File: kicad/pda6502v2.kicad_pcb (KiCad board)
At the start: 4 copper layers, 100 x 100 mm, 89 parts, among them J1 GPIO1, J2 GPIO2, J3 UART, J4 Screw_Terminal_01x02, J5 Conn_02x04_Odd_Even, J6 ICSP, J7 SPI, J8 FPGA_EXT, J9 SID, SW1 SW_Push, U1 W65C02SxP, U10 LT3030, U11 SC28L92A1B, U2 W65C22SxP, U3 W65C22SxP, U4 DS1818, U5 AS6C4008-55PCN, U6 ARMSID, U7 AT25M01, U8 ICE40HX4K-TQ144, U9 TLV1117-33, X1 8 MHz, X2 3.6864 MHz

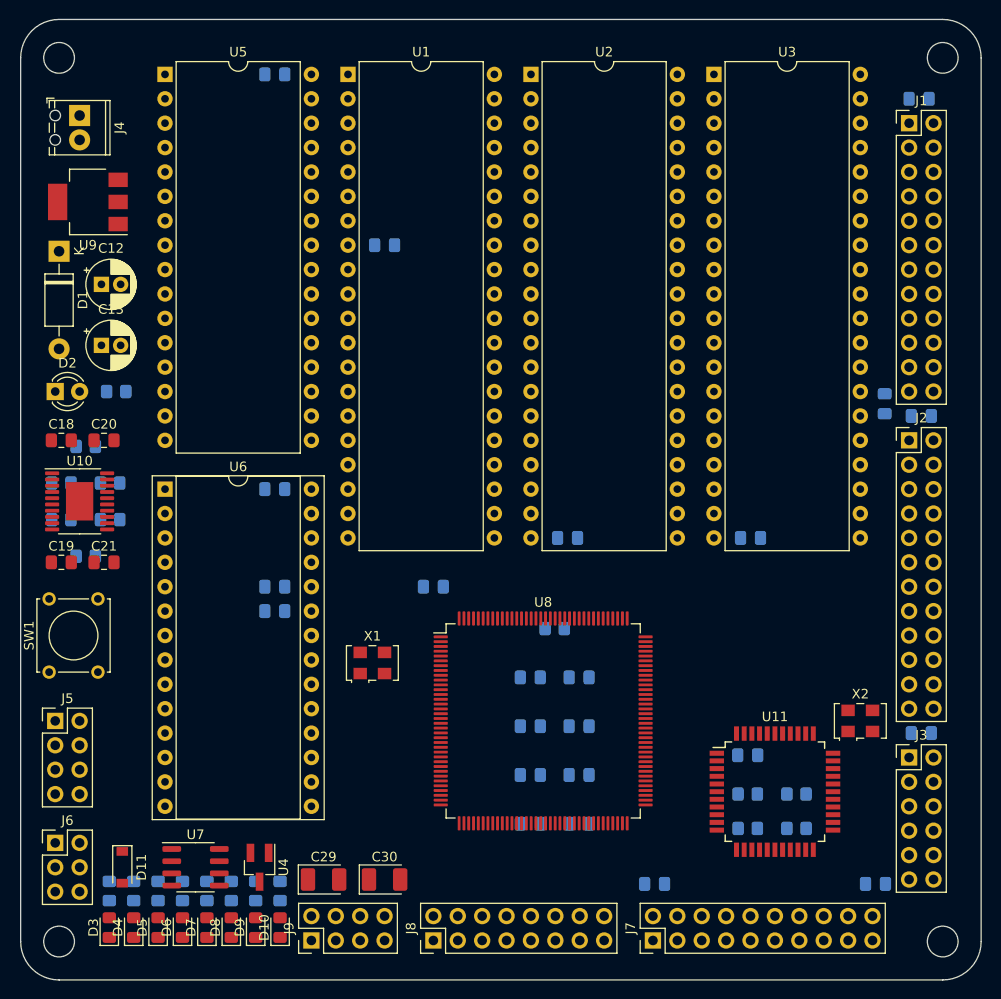
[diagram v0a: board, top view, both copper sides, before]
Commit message: Routing begins; FPGA to EXT & SPI headers.
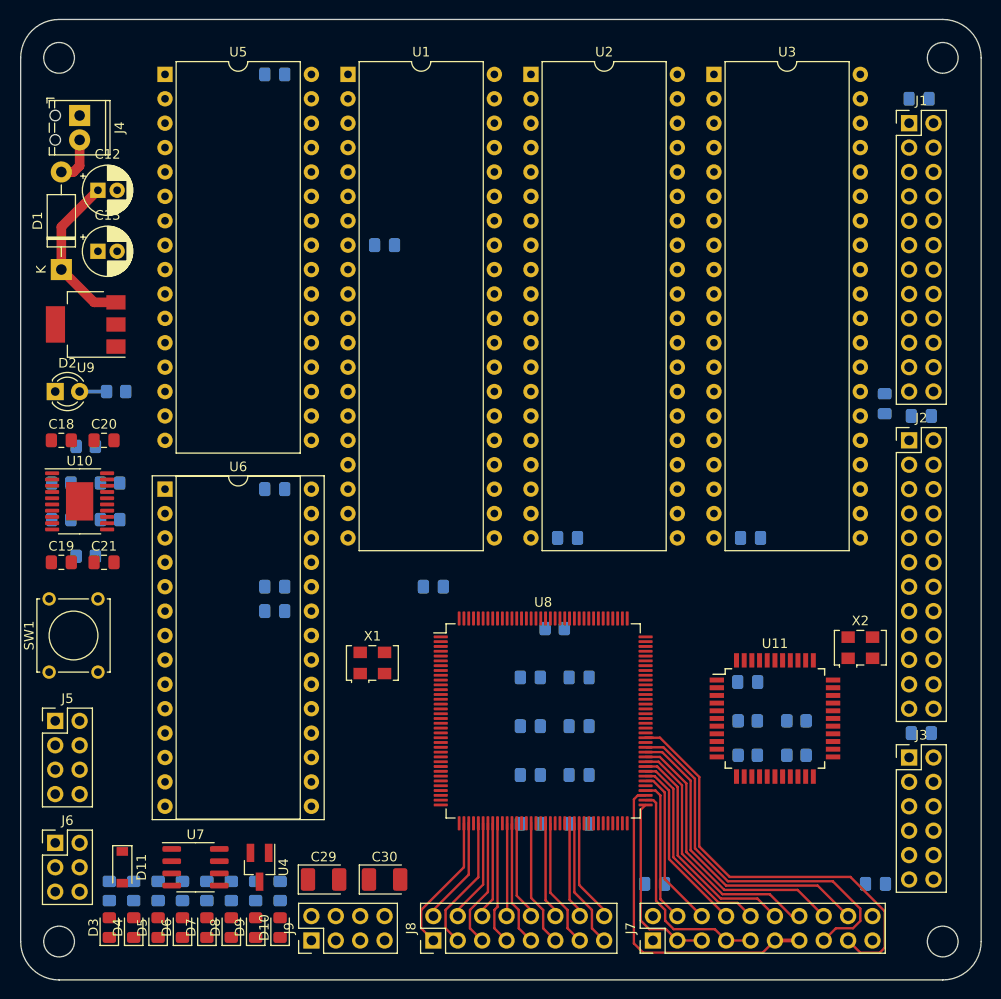
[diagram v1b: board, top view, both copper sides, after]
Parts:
- moved U9 12.8 mm to (104.8, 71.8)
- moved C12 9.80 mm to (106.0, 57.8)
- moved C13 9.80 mm to (106.0, 64.1)
- moved C3 7.62 mm to (173.7, 109.0)
- moved R1 7.62 mm to (173.7, 113.0)
- moved R2 7.62 mm to (178.8, 113.0)
- moved U11 7.62 mm to (176.5, 112.8)
- moved X2 7.62 mm to (185.4, 105.4)
- moved R3 7.62 mm to (173.7, 116.6)
- moved R4 7.62 mm to (178.8, 116.6)
- moved D1 1.92 mm to (102.2, 66.0), turned to 90 degrees
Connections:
- J4 pad 1: Net-(D1-Pad2) -> GND
- J4 pad 2: GND -> Net-(D1-Pad2)
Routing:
- net /SPI_EXP1: track 0.00 -> 45.8 mm
- net /SPI_EXP0: track 0.00 -> 39.5 mm
- net /SPI_CLOCK: track 0.00 -> 34.5 mm
- net /SPI_CS7: track 0.00 -> 32.4 mm
- net /SPI_CS6: track 0.00 -> 29.6 mm
- net /SPI_CS5: track 0.00 -> 26.8 mm
- net /SPI_CS4: track 0.00 -> 24.1 mm
- net /SPI_MOSI: track 0.00 -> 23.6 mm
- net /SPI_CS3: track 0.00 -> 21.3 mm
- net /SPI_MISO: track 0.00 -> 19.5 mm
- net /SPI_CS2: track 0.00 -> 18.6 mm
- net /SPI_CS1: track 0.00 -> 17.6 mm
- net +5V: track 0.00 -> 16.9 mm
- net /SPI_CS0: track 0.00 -> 15.0 mm
- net /EXT_0: track 0.00 -> 14.6 mm
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
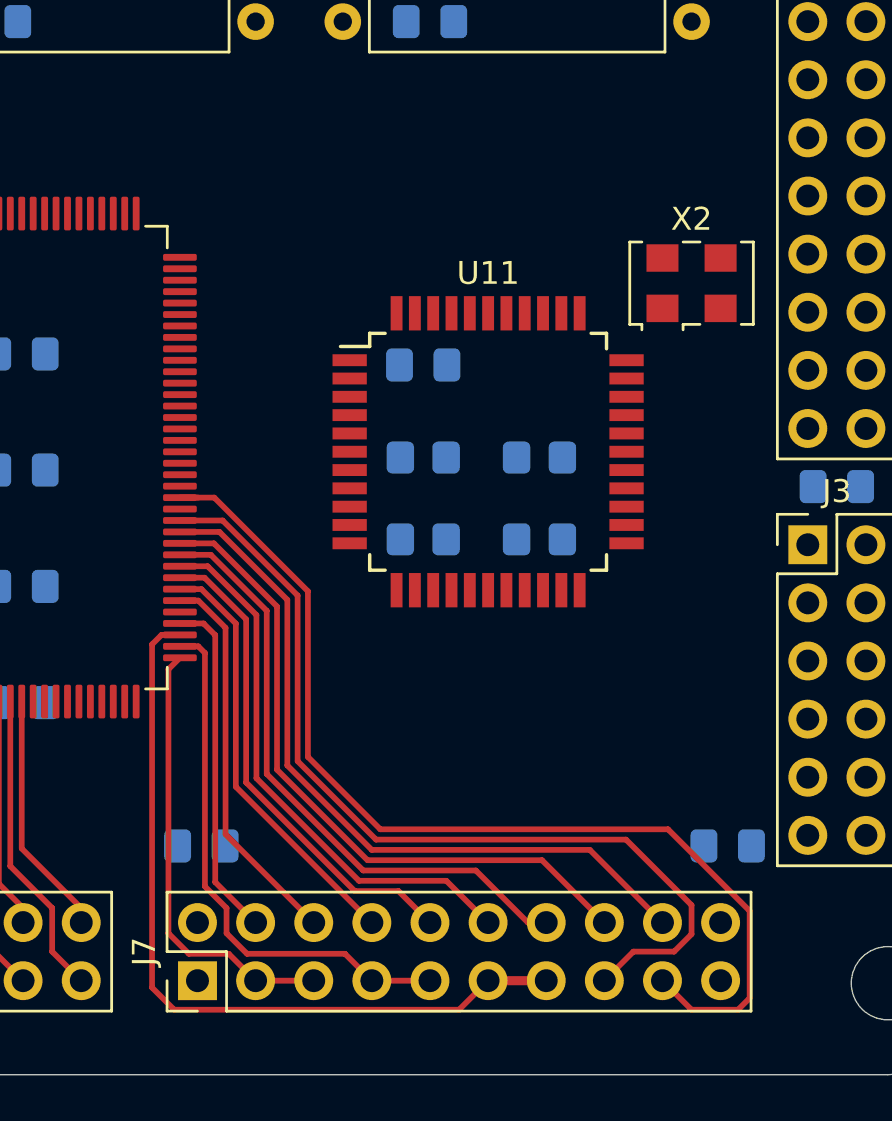
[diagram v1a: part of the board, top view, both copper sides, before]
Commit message: FPGA EXT/SPI routing tweaks, UART moved down/right
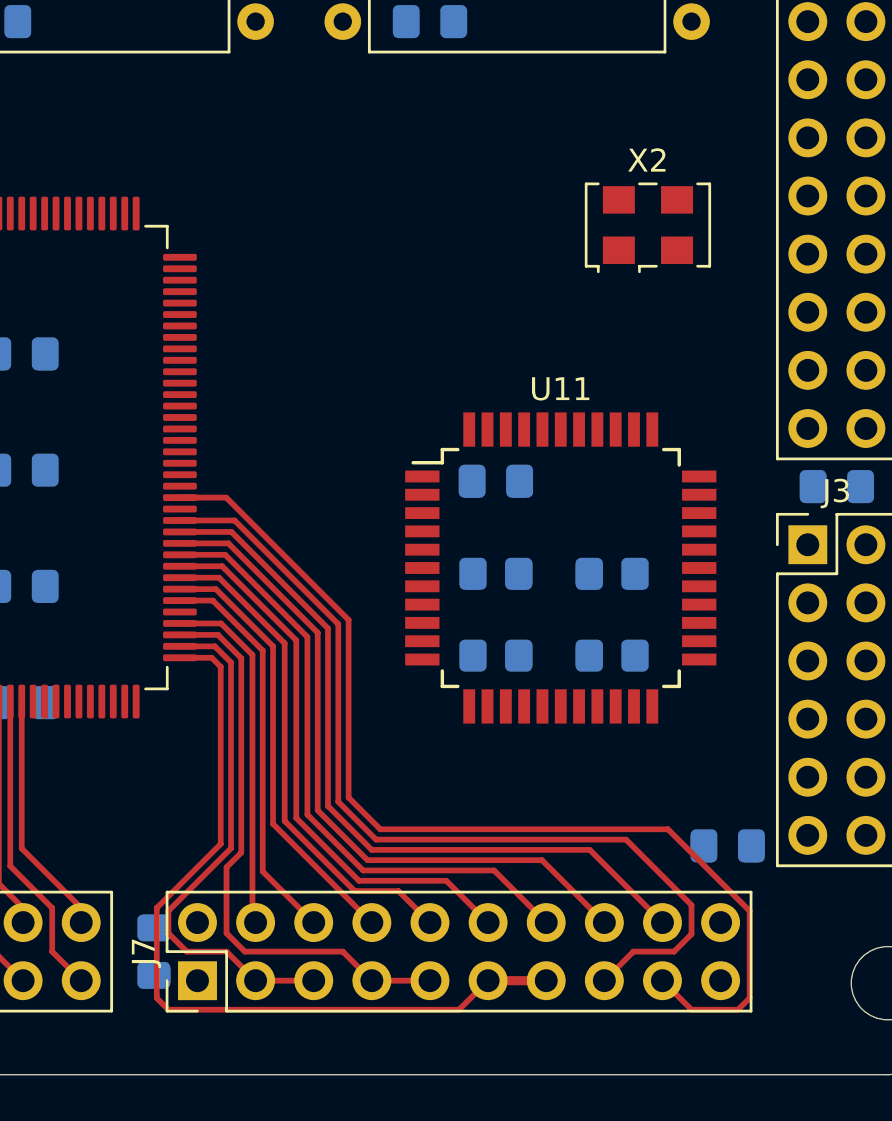
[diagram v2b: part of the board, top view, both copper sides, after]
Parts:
- moved C3 5.99 mm to (176.9, 114.1)
- moved R1 5.99 mm to (176.9, 118.1)
- moved R3 5.99 mm to (176.9, 121.7)
- moved U11 5.99 mm to (179.7, 117.9)
- moved R2 5.99 mm to (181.9, 118.1)
- moved R4 5.99 mm to (181.9, 121.7)
- moved C26 5.06 mm to (161.9, 134.6), turned to 270 degrees
- moved X2 3.17 mm to (183.5, 102.9)
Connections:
- J3 pad 5: (no net) -> Net-(J3-Pad5)
- J3 pad 6: (no net) -> Net-(J3-Pad6)
- U1 pad 3: (no net) -> Net-(U1-Pad3)
- U1 pad 35: (no net) -> Net-(U1-Pad35)
- U1 pad 39: (no net) -> Net-(U1-Pad39)
- U11 pad 23: (no net) -> Net-(U11-Pad23)
- U11 pad 26: (no net) -> Net-(U11-Pad26)
- U11 pad 31: (no net) -> Net-(U11-Pad31)
- U11 pad 34: (no net) -> Net-(U11-Pad34)
- U11 pad 35: (no net) -> Net-(U11-Pad35)
- U11 pad 36: (no net) -> Net-(U11-Pad36)
- U11 pad 37: (no net) -> Net-(U11-Pad37)
- U11 pad 41: (no net) -> Net-(U11-Pad41)
- U11 pad 8: (no net) -> Net-(U11-Pad8)
- U8 pad 101: (no net) -> Net-(U8-Pad101)
- U8 pad 102: (no net) -> Net-(U8-Pad102)
- U8 pad 109: (no net) -> Net-(U8-Pad109)
- U8 pad 12: (no net) -> Net-(U8-Pad12)
- U8 pad 133: (no net) -> Net-(U8-Pad133)
- U8 pad 16: (no net) -> Net-(U8-Pad16)
- U8 pad 17: (no net) -> Net-(U8-Pad17)
- U8 pad 18: (no net) -> Net-(U8-Pad18)
- U8 pad 21: (no net) -> Net-(U8-Pad21)
- U8 pad 35: (no net) -> Net-(U8-Pad35)
- U8 pad 36: (no net) -> Net-(U8-Pad36)
- U8 pad 37: (no net) -> Net-(U8-Pad37)
- U8 pad 50: (no net) -> Net-(U8-Pad50)
- U8 pad 51: (no net) -> Net-(U8-Pad51)
- U8 pad 58: (no net) -> Net-(U8-Pad58)
- U8 pad 63: (no net) -> Net-(U8-Pad63)
- U8 pad 64: (no net) -> Net-(U8-Pad64)
- U8 pad 65: (no net) -> Net-(U8-Pad65)
- U8 pad 73: /SPI_MISO -> /SPI_CLOCK
- U8 pad 74: /SPI_MOSI -> /SPI_MISO
- U8 pad 75: /SPI_CLOCK -> /SPI_MOSI
- U8 pad 77: (no net) -> Net-(U8-Pad77)
- U8 pad 88: (no net) -> Net-(U8-Pad88)
- X1 pad 1: (no net) -> Net-(X1-Pad1)
- X2 pad 1: (no net) -> Net-(X2-Pad1)
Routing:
- net /SPI_MISO: track 19.5 -> 22.7 mm
- net /SPI_MOSI: track 23.6 -> 25.1 mm
- net /SPI_CLOCK: track 34.5 -> 35.3 mm

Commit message: Routing WIP; UART
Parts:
- R3, R4: moved to F.Cu
- moved X2 22.9 mm to (184.9, 125.7), turned to 90 degrees
- moved R4 10.0 mm to (172.2, 119.4), turned to 270 degrees
- moved R1 9.54 mm to (180.3, 109.2)
- moved R3 7.15 mm to (183.6, 119.4), turned to 270 degrees
- moved R23 5.96 mm to (157.5, 108.0)
- moved C22 5.78 mm to (157.5, 113.0)
- moved C11 5.73 mm to (152.3, 118.2)
- moved C17 5.73 mm to (157.4, 118.2)
- moved U11 5.38 mm to (177.9, 112.8)
- moved C3 5.38 mm to (175.1, 109.0)
- moved R2 5.38 mm to (180.2, 113.0)
- moved C27 4.93 mm to (188.7, 134.6), turned to 270 degrees
- moved C14 3.84 mm to (147.2, 118.2)
- moved C15 3.84 mm to (147.2, 113.1)
- moved C16 3.84 mm to (147.2, 108.0)
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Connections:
- U8 pad 97: /UART_~CS -> /UART_TXA~IRQ
- U8 pad 98: /UART_TXA~IRQ -> /UART_RXA~IRQ
- U8 pad 99: /UART_RXA~IRQ -> /UART_~CS
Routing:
- net /UART_~IRQ: track 0.00 -> 35.0 mm
- net /UART_~CS: track 0.00 -> 25.6 mm
- net /UART_TXA~IRQ: track 0.00 -> 25.0 mm
- net /UART_RXA~IRQ: track 0.00 -> 24.8 mm
- net Net-(U11-Pad30): track 0.00 -> 15.5 mm
- net /UART_TXB~IRQ: track 0.00 -> 10.6 mm
- net /UART_IM: track 0.00 -> 10.5 mm
- net /UART_RXB~IRQ: track 0.00 -> 10.4 mm
- net /UART_~RDN: track 0.00 -> 8.98 mm
- net /D6: track 0.00 -> 8.96 mm, vias 0 -> 1
- net /D2: track 0.00 -> 8.95 mm, vias 0 -> 1
- net /UART_~WRN: track 0.00 -> 8.85 mm
- net /D0: track 0.00 -> 8.20 mm, vias 0 -> 1
- net /D4: track 0.00 -> 8.18 mm, vias 0 -> 1
- net /D1: track 0.00 -> 6.93 mm, vias 0 -> 1
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- added copper zone on In2.Cu, net +3V3
- added copper zone on B.Cu, net GND
- added copper zone on F.Cu, net GND
- added copper zone on In1.Cu, net GND

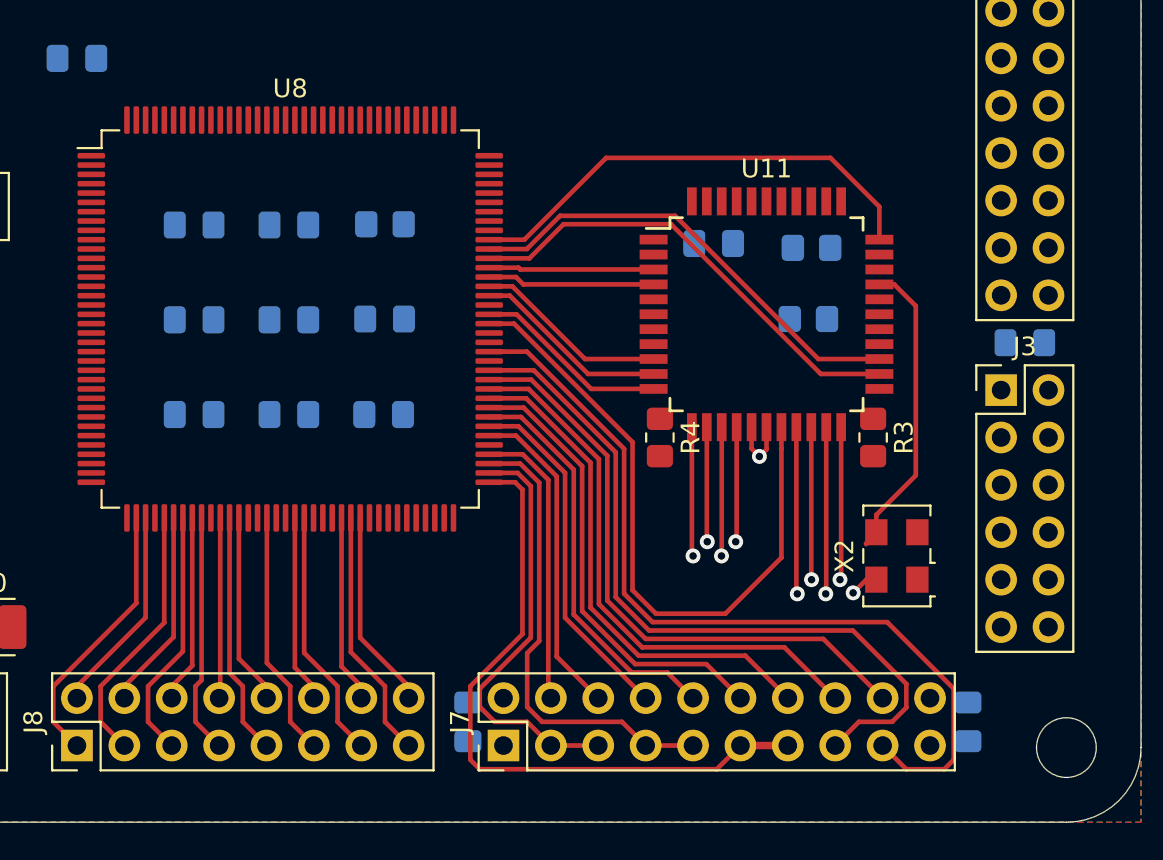
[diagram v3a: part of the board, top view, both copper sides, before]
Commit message: Routing WIP: UART header, caps/resistors etc.
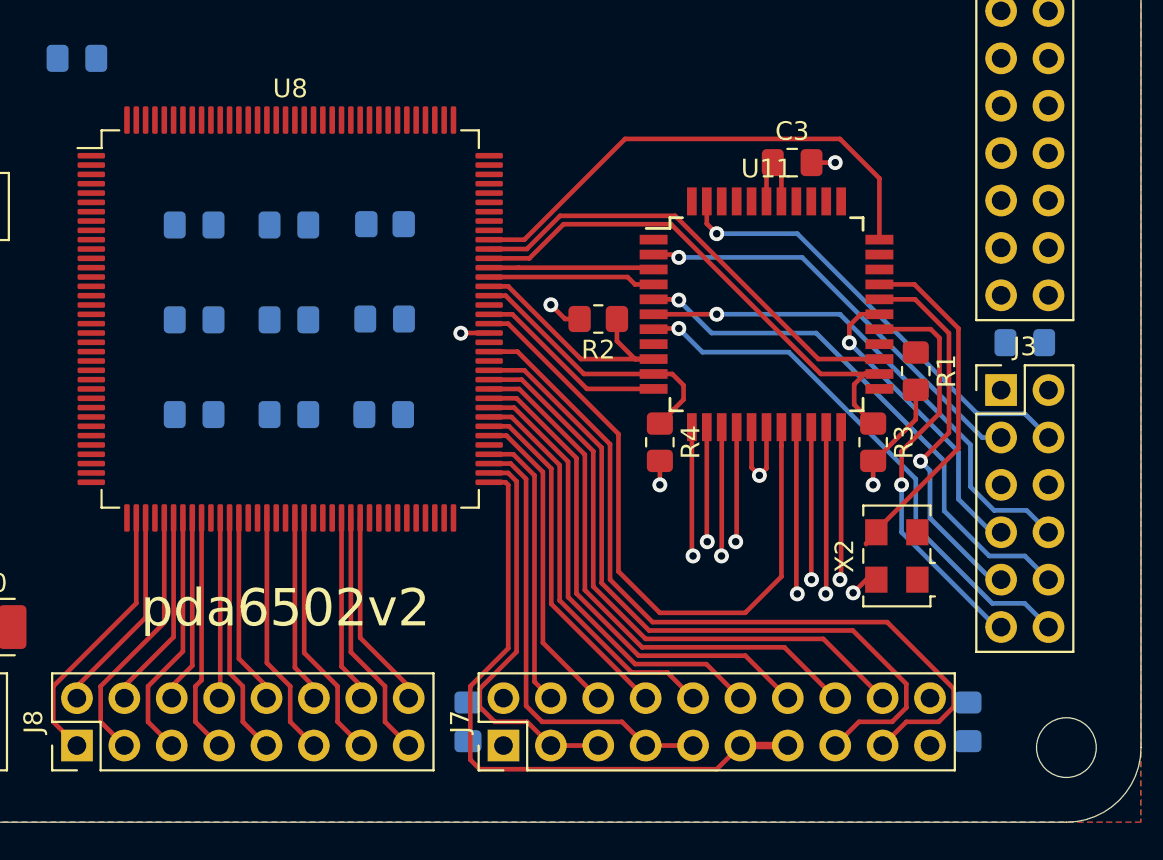
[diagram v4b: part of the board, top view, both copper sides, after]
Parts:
- C3, R1, R2: moved to F.Cu
- moved R2 11.3 mm to (168.9, 113.0), turned to 180 degrees
- moved R1 8.65 mm to (185.9, 115.8), turned to 270 degrees
- moved C3 6.04 mm to (179.3, 104.6)
- moved R3 0.25 mm to (183.6, 119.6)
- moved R4 0.25 mm to (172.2, 119.6)
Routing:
- net /UARTB_RTS: track 0.00 -> 29.3 mm, vias 0 -> 1
- net /UARTB_RX: track 0.00 -> 29.0 mm, vias 0 -> 1
- net /UARTB_TX: track 0.00 -> 27.3 mm, vias 0 -> 1
- net /UARTB_CTS: track 0.00 -> 24.3 mm, vias 0 -> 1
- net /UARTA_CTS: track 0.00 -> 22.7 mm, vias 0 -> 1
- net /UARTA_RTS: track 0.00 -> 22.4 mm, vias 0 -> 1
- net /UARTA_RX: track 0.00 -> 20.4 mm, vias 0 -> 1
- net /UARTA_TX: track 0.00 -> 16.6 mm, vias 0 -> 1
- net +3V3: track 1.53 -> 16.8 mm, vias 1 -> 5
- net /UART_TXB~IRQ: track 10.6 -> 15.0 mm
- net /UART_TXA~IRQ: track 25.0 -> 29.2 mm
- net /UART_RXB~IRQ: track 10.4 -> 14.0 mm
- net GND: track 3.47 -> 6.77 mm, vias 1 -> 2
- net /SPI_EXP1: track 46.1 -> 43.1 mm
- net Net-(U11-Pad30): track 15.5 -> 18.0 mm
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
